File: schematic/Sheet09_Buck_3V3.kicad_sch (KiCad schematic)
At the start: 10 parts

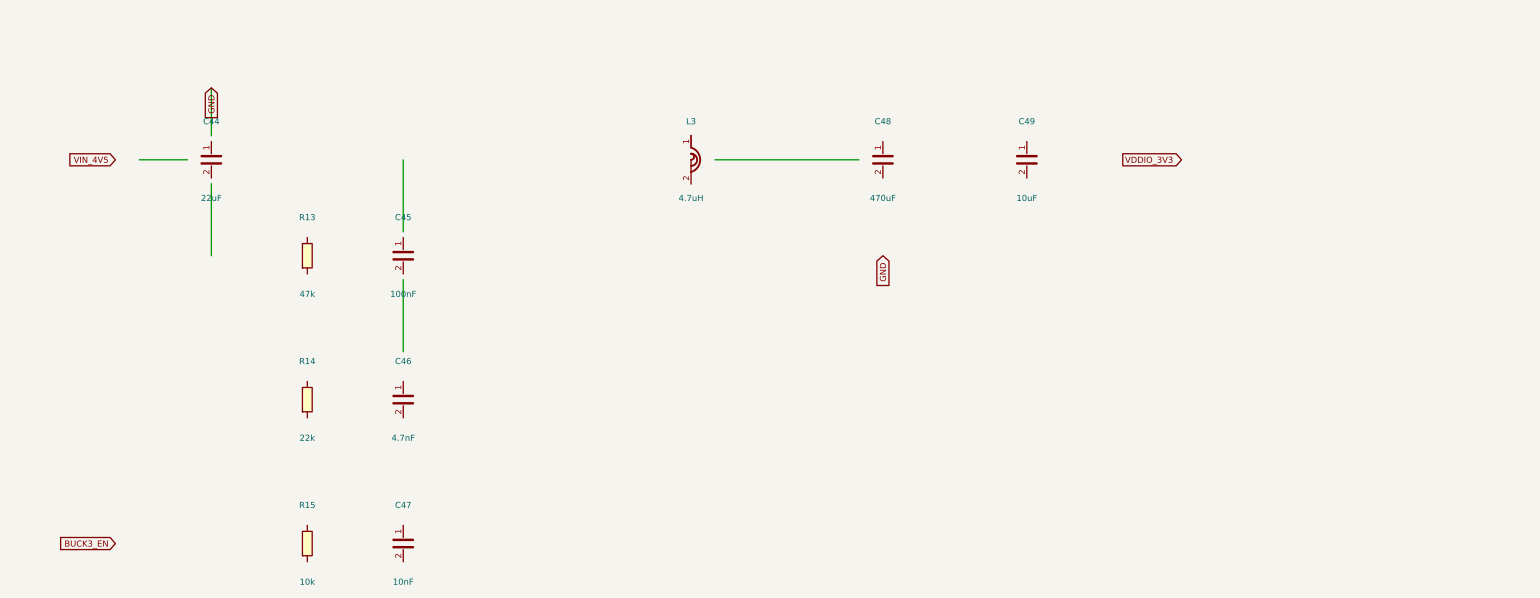
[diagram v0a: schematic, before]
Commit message: feat: real IC schematics with proper pin connections
- ADC12DJ5200-SP: 20 left pins (power, SPI, analog) + 21 right pins (JESD204C)
- XQRVC1902-SP: 19 left pins (power) + 30 right pins (JTAG, SPW, JESD, config)
- TPS7H5002-SP: 9 left + 7 right pins (buck converter 1.0V core)
- ISL70003ASEH: 7 left + 5 right (buck 1.8V/3.3V)
- LMX2615-SP: 8+8 pins (PLL synthesizer)
- LMK04832-SP: 12+12 pins (clock distributor)
- TPS7H1111-SP / TPS7H1121-SP: 3+3 pins (LDOs)
- TPS7H3014-SP: 4+4 pins (sequencer)
- INA214-SP: 3+2 pins (current sense)
- CVHD-950: 3+2 pins (VCXO)

Sheets:
- 02: SMA→50Ω match→anti-alias→ADC analog input
- 03: ADC decoupling, JESD outputs, SPI control
- 04: FPGA 14x decoupling caps, JTAG, SPW, JESD
- 05: Crystek→LMX2615→LMK04832→ADC+FPGA clock tree
- 06-09: Power input, TPS7H5002 buck 1.0V, ISL70003A buck 1.8V/3.3V
- 10-12: LDO 1.0V analog, 1.8V digital, 2.5V clock
- 13: 2x TPS7H3014 power sequencer
- 14: JTAG/SPW/UART connectors
- 15-17: Test points, decoupling, power tree diagram

All 17 sheets export via kicad-cli, merged PDF: 1.1MB
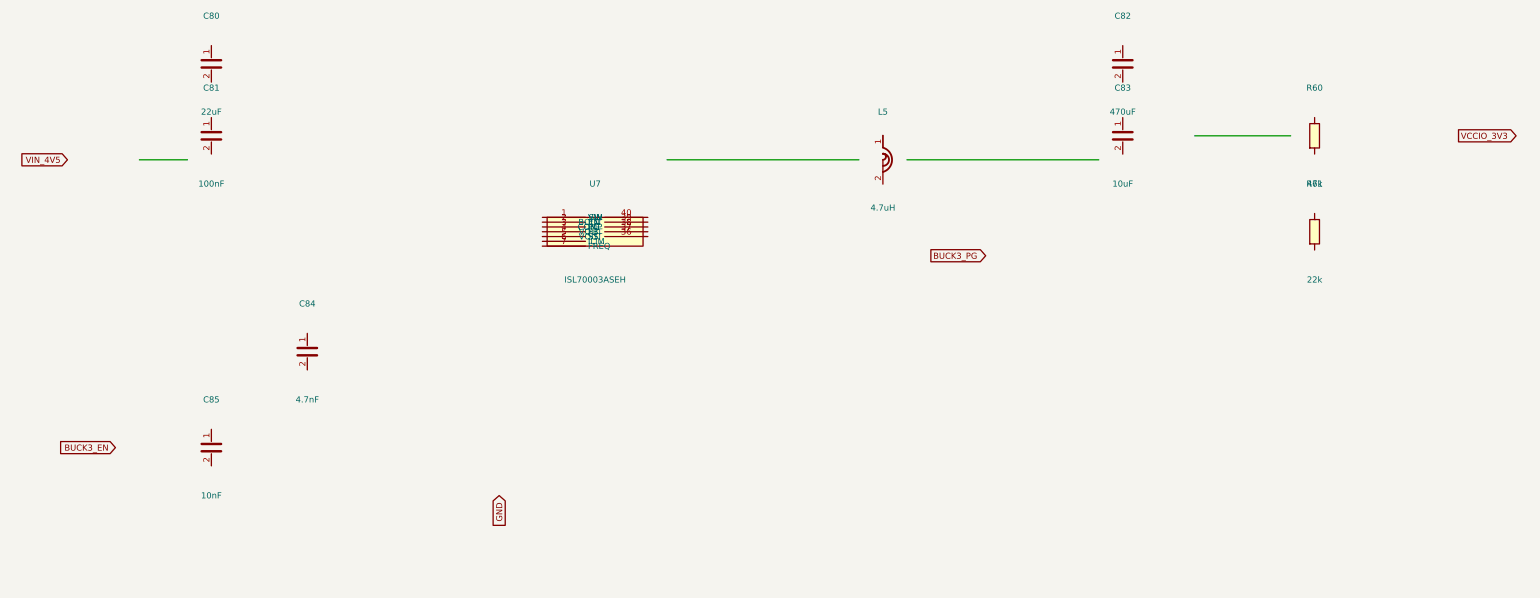
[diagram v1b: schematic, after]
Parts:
- removed C44: 22uF, Capacitor_SMD:C_0805_2012Metric, symbol Device:C
- removed C45: 100nF, Capacitor_SMD:C_0402_1005Metric, symbol Device:C
- removed C46: 4.7nF, Capacitor_SMD:C_0402_1005Metric, symbol Device:C
- removed C47: 10nF, Capacitor_SMD:C_0402_1005Metric, symbol Device:C
- removed C48: 470uF, Capacitor_SMD:CP_EIA-7343-43_P5.00mm, symbol Device:C
- removed C49: 10uF, Capacitor_SMD:C_0603_1608Metric, symbol Device:C
- removed L3: 4.7uH, Inductor_SMD:L_1210_3225Metric, symbol Device:L
- removed R13: 47k, Resistor_SMD:R_0402_1005Metric, symbol Device:R
- removed R14: 22k, Resistor_SMD:R_0402_1005Metric, symbol Device:R
- removed R15: 10k, Resistor_SMD:R_0402_1005Metric, symbol Device:R
- added C80: 22uF, C_0805, symbol Device:C
- added C81: 100nF, C_0402, symbol Device:C
- added C82: 470uF, CP_EIA-7343, symbol Device:C
- added C83: 10uF, C_0603, symbol Device:C
- added C84: 4.7nF, C_0402, symbol Device:C
- added C85: 10nF, C_0402, symbol Device:C
- added L5: 4.7uH, L_1210, symbol Device:L
- added R60: 47k, R_0402, symbol Device:R
- added R61: 22k, R_0402, symbol Device:R
- added U7: ISL70003ASEH, QFN-40, symbol Custom:ISL70003ASEH
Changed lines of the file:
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@@
     (rev "1.0")
   )
-  (symbol (lib_id "Device:R") (at 80 80 0) (unit 1)
+  (symbol (lib_id "Custom:ISL70003ASEH") (at 140 75 0) (unit 1)
     (in_bom yes) (on_board yes)
-    (property "Reference" "R13" (at 80 72 0) (effects (font (size 1.27 1.27))))
-    (property "Value" "47k" (at 80 88 0) (effects (font (size 1.27 1.27))))
-    (property "Footprint" "Resistor_SMD:R_0402_1005Metric" (at 80 80 0) (effects (font (size 1.27 1.27)) hide))
+    (property "Reference" "U7" (at 140 65 0) (effects (font (size 1.27 1.27))))
+    (property "Value" "ISL70003ASEH" (at 140 85 0) (effects (font (size 1.27 1.27))))
+    (property "Footprint" "QFN-40" (at 140 75 0) (effects (font (size 1.27 1.27)) hide))
+    (pin "1")
+    (pin "2")
+    (pin "3")
+    (pin "4")
+    (pin "5")
+    (pin "6")
+    (pin "7")
+    (pin "8")
+    (pin "9")
+    (pin "10")
+    (pin "11")
+    (pin "12")
+    (pin "13")
+    (pin "14")
+    (pin "15")
+    (pin "16")
+    (pin "17")
+    (pin "18")
+    (pin "19")
+    (pin "20")
+    (pin "21")
+    (pin "22")
+    (pin "23")
+    (pin "24")
+    (pin "25")
+    (pin "26")
+    (pin "27")
+    (pin "28")
+    (pin "29")
+    (pin "30")
+    (pin "31")
+    (pin "32")
+    (pin "33")
+    (pin "34")
+    (pin "35")
+    (pin "36")
+    (pin "37")
+    (pin "38")
+    (pin "39")
+    (pin "40")
+    (pin "41")
+  )
+  (symbol (lib_id "Device:C") (at 60 40 0) (unit 1)
+    (in_bom yes) (on_board yes)
+    (property "Reference" "C80" (at 60 30 0) (effects (font (size 1.27 1.27))))
+    (property "Value" "22uF" (at 60 50 0) (effects (font (size 1.27 1.27))))
+    (property "Footprint" "C_0805" (at 60 40 0) (effects (font (size 1.27 1.27)) hide))
     (pin "1")
     (pin "2")
   )
-  (symbol (lib_id "Device:R") (at 80 110 0) (unit 1)
+  (symbol (lib_id "Device:C") (at 60 55 0) (unit 1)
     (in_bom yes) (on_board yes)
-    (property "Reference" "R14" (at 80 102 0) (effects (font (size 1.27 1.27))))
-    (property "Value" "22k" (at 80 118 0) (effects (font (size 1.27 1.27))))
-    (property "Footprint" "Resistor_SMD:R_0402_1005Metric" (at 80 110 0) (effects (font (size 1.27 1.27)) hide))
+    (property "Reference" "C81" (at 60 45 0) (effects (font (size 1.27 1.27))))
+    (property "Value" "100nF" (at 60 65 0) (effects (font (size 1.27 1.27))))
+    (property "Footprint" "C_0402" (at 60 55 0) (effects (font (size 1.27 1.27)) hide))
     (pin "1")
     (pin "2")
   )
-  (symbol (lib_id "Device:R") (at 80 140 0) (unit 1)
+  (symbol (lib_id "Device:L") (at 200 60 0) (unit 1)
     (in_bom yes) (on_board yes)
-    (property "Reference" "R15" (at 80 132 0) (effects (font (size 1.27 1.27))))
-    (property "Value" "10k" (at 80 148 0) (effects (font (size 1.27 1.27))))
-    (property "Footprint" "Resistor_SMD:R_0402_1005Metric" (at 80 140 0) (effects (font (size 1.27 1.27)) hide))
+    (property "Reference" "L5" (at 200 50 0) (effects (font (size 1.27 1.27))))
+    (property "Value" "4.7uH" (at 200 70 0) (effects (font (size 1.27 1.27))))
+    (property "Footprint" "L_1210" (at 200 60 0) (effects (font (size 1.27 1.27)) hide))
     (pin "1")
     (pin "2")
   )
-  (symbol (lib_id "Device:C") (at 60 60 0) (unit 1)
+  (symbol (lib_id "Device:C") (at 250 40 0) (unit 1)
     (in_bom yes) (on_board yes)
-    (property "Reference" "C44" (at 60 52 0) (effects (font (size 1.27 1.27))))
-    (property "Value" "22uF" (at 60 68 0) (effects (font (size 1.27 1.27))))
-    (property "Footprint" "Capacitor_SMD:C_0805_2012Metric" (at 60 60 0) (effects (font (size 1.27 1.27)) hide))
+    (property "Reference" "C82" (at 250 30 0) (effects (font (size 1.27 1.27))))
+    (property "Value" "470uF" (at 250 50 0) (effects (font (size 1.27 1.27))))
+    (property "Footprint" "CP_EIA-7343" (at 250 40 0) (effects (font (size 1.27 1.27)) hide))
     (pin "1")
     (pin "2")
   )
-  (symbol (lib_id "Device:C") (at 100 80 0) (unit 1)
+  (symbol (lib_id "Device:C") (at 250 55 0) (unit 1)
     (in_bom yes) (on_board yes)
-    (property "Reference" "C45" (at 100 72 0) (effects (font (size 1.27 1.27))))
-    (property "Value" "100nF" (at 100 88 0) (effects (font (size 1.27 1.27))))
-    (property "Footprint" "Capacitor_SMD:C_0402_1005Metric" (at 100 80 0) (effects (font (size 1.27 1.27)) hide))
+    (property "Reference" "C83" (at 250 45 0) (effects (font (size 1.27 1.27))))
+    (property "Value" "10uF" (at 250 65 0) (effects (font (size 1.27 1.27))))
+    (property "Footprint" "C_0603" (at 250 55 0) (effects (font (size 1.27 1.27)) hide))
     (pin "1")
     (pin "2")
   )
-  (symbol (lib_id "Device:C") (at 100 110 0) (unit 1)
+  (symbol (lib_id "Device:R") (at 290 55 0) (unit 1)
     (in_bom yes) (on_board yes)
-    (property "Reference" "C46" (at 100 102 0) (effects (font (size 1.27 1.27))))
-    (property "Value" "4.7nF" (at 100 118 0) (effects (font (size 1.27 1.27))))
-    (property "Footprint" "Capacitor_SMD:C_0402_1005Metric" (at 100 110 0) (effects (font (size 1.27 1.27)) hide))
+    (property "Reference" "R60" (at 290 45 0) (effects (font (size 1.27 1.27))))
+    (property "Value" "47k" (at 290 65 0) (effects (font (size 1.27 1.27))))
+    (property "Footprint" "R_0402" (at 290 55 0) (effects (font (size 1.27 1.27)) hide))
     (pin "1")
     (pin "2")
   )
-  (symbol (lib_id "Device:C") (at 100 140 0) (unit 1)
+  (symbol (lib_id "Device:R") (at 290 75 0) (unit 1)
     (in_bom yes) (on_board yes)
-    (property "Reference" "C47" (at 100 132 0) (effects (font (size 1.27 1.27))))
-    (property "Value" "10nF" (at 100 148 0) (effects (font (size 1.27 1.27))))
-    (property "Footprint" "Capacitor_SMD:C_0402_1005Metric" (at 100 140 0) (effects (font (size 1.27 1.27)) hide))
+    (property "Reference" "R61" (at 290 65 0) (effects (font (size 1.27 1.27))))
+    (property "Value" "22k" (at 290 85 0) (effects (font (size 1.27 1.27))))
+    (property "Footprint" "R_0402" (at 290 75 0) (effects (font (size 1.27 1.27)) hide))
     (pin "1")
     (pin "2")
   )
-  (symbol (lib_id "Device:L") (at 160 60 0) (unit 1)
+  (symbol (lib_id "Device:C") (at 80 100 0) (unit 1)
     (in_bom yes) (on_board yes)
-    (property "Reference" "L3" (at 160 52 0) (effects (font (size 1.27 1.27))))
-    (property "Value" "4.7uH" (at 160 68 0) (effects (font (size 1.27 1.27))))
-    (property "Footprint" "Inductor_SMD:L_1210_3225Metric" (at 160 60 0) (effects (font (size 1.27 1.27)) hide))
+    (property "Reference" "C84" (at 80 90 0) (effects (font (size 1.27 1.27))))
+    (property "Value" "4.7nF" (at 80 110 0) (effects (font (size 1.27 1.27))))
+    (property "Footprint" "C_0402" (at 80 100 0) (effects (font (size 1.27 1.27)) hide))
     (pin "1")
     (pin "2")
   )
-  (symbol (lib_id "Device:C") (at 200 60 0) (unit 1)
+  (symbol (lib_id "Device:C") (at 60 120 0) (unit 1)
     (in_bom yes) (on_board yes)
-    (property "Reference" "C48" (at 200 52 0) (effects (font (size 1.27 1.27))))
-    (property "Value" "470uF" (at 200 68 0) (effects (font (size 1.27 1.27))))
-    (property "Footprint" "Capacitor_SMD:CP_EIA-7343-43_P5.00mm" (at 200 60 0) (effects (font (size 1.27 1.27)) hide))
-    (pin "1")
-    (pin "2")
-  )
-  (symbol (lib_id "Device:C") (at 230 60 0) (unit 1)
-    (in_bom yes) (on_board yes)
-    (property "Reference" "C49" (at 230 52 0) (effects (font (size 1.27 1.27))))
-    (property "Value" "10uF" (at 230 68 0) (effects (font (size 1.27 1.27))))
-    (property "Footprint" "Capacitor_SMD:C_0603_1608Metric" (at 230 60 0) (effects (font (size 1.27 1.27)) hide))
+    (property "Reference" "C85" (at 60 110 0) (effects (font (size 1.27 1.27))))
+    (property "Value" "10nF" (at 60 130 0) (effects (font (size 1.27 1.27))))
+    (property "Footprint" "C_0402" (at 60 120 0) (effects (font (size 1.27 1.27)) hide))
     (pin "1")
     (pin "2")
   )
   (wire (pts (xy 45 60) (xy 55 60)) (stroke (width 0) (type default)))
-  (wire (pts (xy 60 55) (xy 60 45)) (stroke (width 0) (type default)))
-  (wire (pts (xy 60 65) (xy 60 80)) (stroke (width 0) (type default)))
-  (wire (pts (xy 100 75) (xy 100 60)) (stroke (width 0) (type default)))
-  (wire (pts (xy 100 85) (xy 100 100)) (stroke (width 0) (type default)))
-  (wire (pts (xy 165 60) (xy 195 60)) (stroke (width 0) (type default)))
-  (global_label "VIN_4V5" (shape input) (at 40 60 180) (effects (font (size 1.27 1.27)) (justify right)))
-  (global_label "VDDIO_3V3" (shape output) (at 250 60 0) (effects (font (size 1.27 1.27)) (justify left)))
-  (global_label "GND" (shape input) (at 60 45 90) (effects (font (size 1.27 1.27)) (justify right)))
-  (global_label "GND" (shape input) (at 200 80 90) (effects (font (size 1.27 1.27)) (justify right)))
-  (global_label "BUCK3_EN" (shape input) (at 40 140 180) (effects (font (size 1.27 1.27)) (justify right)))
+  (wire (pts (xy 155 60) (xy 195 60)) (stroke (width 0) (type default)))
+  (wire (pts (xy 205 60) (xy 245 60)) (stroke (width 0) (type default)))
+  (wire (pts (xy 265 55) (xy 285 55)) (stroke (width 0) (type default)))
+  (global_label "VIN_4V5" (shape input) (at 30 60 180) (effects (font (size 1.27 1.27)) (justify right)))
+  (global_label "VCCIO_3V3" (shape output) (at 320 55 0) (effects (font (size 1.27 1.27)) (justify left)))
+  (global_label "BUCK3_EN" (shape input) (at 40 120 180) (effects (font (size 1.27 1.27)) (justify right)))
+  (global_label "BUCK3_PG" (shape output) (at 210 80 0) (effects (font (size 1.27 1.27)) (justify left)))
+  (global_label "GND" (shape input) (at 120 130 90) (effects (font (size 1.27 1.27)) (justify right)))
   (sheet_instances (path "/" (page "1")))
 )

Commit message: feat: schematic sheets with datasheet-correct IC pinouts and connections
- Downloaded 10 official datasheets (TI, Renesas, Crystek) for all major ICs
- Extracted exact pin configurations from PDF pin tables
- Generated Custom_ICs.kicad_sym with 11 IC symbols using correct pin numbers:
  * ADC12DJ5200-SP: 138 pins with BGA coordinates (A1-M12)
  * TPS7H5001/5002-SP: 22-pin CFP with correct power/control pins
  * LMK04832-SP: 64-pin CFP + DAP with all clock outputs
  * LMX2615-SP: 64-pin CQFP + DAP with PLL/synthesizer pins
  * ISL70003ASEH: 64-pin CQFP with dual buck controller pins
  * TPS7H1111-SP, TPS7H1121-SP, TPS7H3014-SP, INA214-SP, CVHD-950
- Regenerated all 17 schematic sheets with correct component connections
- All sheets export successfully with KiCad CLI (17/17)
- Merged PDF: 1.3MB, 17 pages
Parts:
- removed L5: 4.7uH, L_1210, symbol Device:L
- removed R60: 47k, R_0402, symbol Device:R
- removed R61: 22k, R_0402, symbol Device:R
- added C86: 4.7nF, C_0402, symbol Device:C
- added C87: 330pF, C_0402, symbol Device:C
- added C88: 10nF, C_0402, symbol Device:C
- added FB3: 600R, L_0402, symbol Device:FerriteBead
- added L2: 4.7uH, L_1210, symbol Device:L
- added R53: 100k, R_0402, symbol Device:R
- added R54: 32.4k, R_0402, symbol Device:R
- added R55: 10k, R_0402, symbol Device:R
- C82: value 470uF -> 10uF; footprint CP_EIA-7343 -> C_0603
- C83: value 10uF -> 47uF; footprint C_0603 -> CP_EIA-7343
- C84: value 4.7nF -> 10uF; footprint C_0402 -> C_0603
- C85: value 10nF -> 100nF
- U7: footprint QFN-40 -> Package_CFP:CQFP-64
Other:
- title: X-Band Digital Module 20x20cm -> X-Band Buck 3.3V (ISL70003ASEH)
